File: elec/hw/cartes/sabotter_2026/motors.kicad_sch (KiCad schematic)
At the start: 3 parts

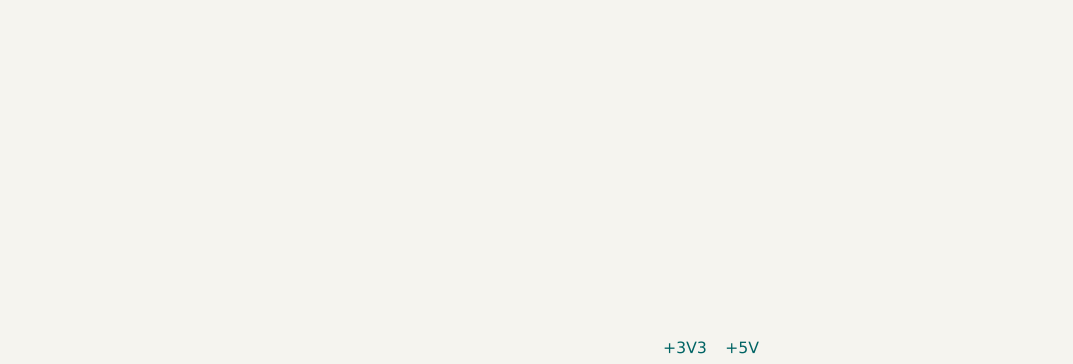
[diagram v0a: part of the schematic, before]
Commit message: switchs added to motor ribbon cable
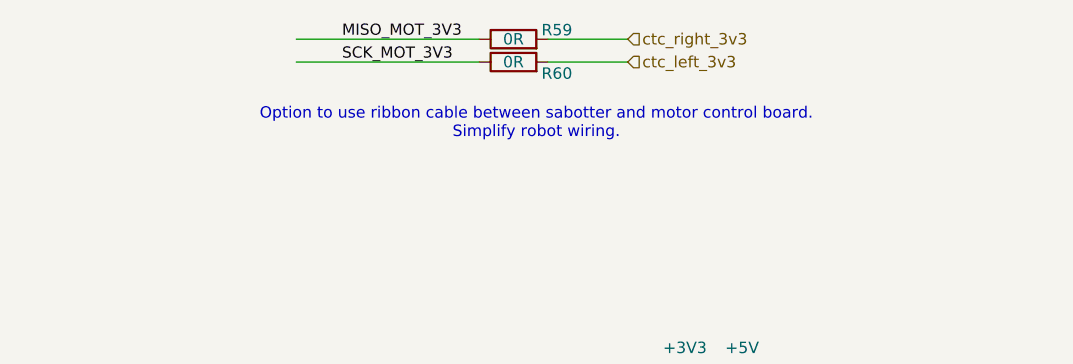
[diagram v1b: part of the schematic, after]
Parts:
- added R59, R60: 0R, cocotter_resistor:r0603_reflow, symbol cocotter_resistors:R_0R_0603
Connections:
- net miso_mot_3v3: now also R59.1
- net sck_mot_3v3: now also R60.1
- new net ctc_left_3v3: R60.2
- new net ctc_right_3v3: R59.2
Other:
- note added: "Option to use ribbon cable between sabotter and motor control board. Simplify robot wiring."

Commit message: sabotter wip
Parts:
- removed R59, R60: 0R, cocotter_resistor:r0603_reflow, symbol cocotter_resistors:R_0R_0603
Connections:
- net nCS_mot1_3v3 is gone; now on net scl_tof_3v3: J15.16 (nCS_3v3)
- net nCS_mot2_3v3 is gone; now on net scl_tof_3v3: J16.16 (nCS_3v3)
- net miso_mot_3v3 renamed irq0_3v3
- net mosi_mot_3v3 renamed irq1_3v3
- net nCS_mot0_3v3 renamed scl_tof_3v3
- net sck_mot_3v3 renamed sda_tof_3v3
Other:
- note removed: "Option to use ribbon cable between sabotter and motor control board. Simplify robot wiring."

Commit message: sabotter wip
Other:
- note added: "ou connecter les irq tof ?"
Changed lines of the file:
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@@
+		)
+	)
+	(text "ou connecter les irq tof ?\n"
+		(exclude_from_sim no)
+		(at 77.216 153.416 0)
+		(effects
+			(font
+				(size 1.27 1.27)
+			)
 		)
 	)

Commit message: tof irq added, needs routing
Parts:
- added R66, R67: 0R, cocotter_resistor:r0603_reflow, symbol cocotter_resistors:R_0R_0603
- added R68: 91k 1%, cocotter_resistor:r0603_reflow, symbol cocotter_resistors:R_91k_0603_1%
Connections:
- net +3V3: now also R68.1
- net irq0_3v3: now also R66.1
- net irq1_3v3: now also R67.1
- new net tof_irq_3v3: R66.2, R67.2, R68.2

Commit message: sabotter corrections wip
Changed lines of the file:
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@@
+		)
+	)
+	(label "irq1_3v3"
+		(at 149.86 116.84 0)
+		(effects
+			(font
+				(size 1.27 1.27)
+			)
+			(justify left bottom)
 		)
 	)
@@
 		)
 	)
+	(label "irq1_3v3"
+		(at 224.79 118.11 0)
+		(effects
+			(font
+				(size 1.27 1.27)
+			)
+			(justify left bottom)
+		)
+	)
 	(label "brake_mot_3v3"
 		(at 144.78 91.44 0)
@@
 		)
 	)
+	(label "irq0_3v3"
+		(at 224.79 115.57 0)
+		(effects
+			(font
+				(size 1.27 1.27)
+			)
+			(justify left bottom)
+		)
+	)
 	(label "GND"
 		(at 151.13 104.14 0)
@@
 			(font
 				(size 1.2446 1.2446)
+			)
+			(justify left bottom)
+		)
+	)
+	(label "irq0_3v3"
+		(at 149.86 114.3 0)
+		(effects
+			(font
+				(size 1.27 1.27)
 			)
 			(justify left bottom)
@@
 		)
 	)
-	(hierarchical_label "irq1_3v3"
-		(shape output)
-		(at 160.02 116.84 0)
-		(effects
-			(font
-				(size 1.27 1.27)
-			)
-			(justify left)
-		)
-	)
 	(hierarchical_label "scl_tof_3v3"
 		(shape input)
 		(at 53.34 121.92 0)
-		(effects
-			(font
-				(size 1.27 1.27)
-			)
-			(justify left)
-		)
-	)
-	(hierarchical_label "irq0_3v3"
-		(shape output)
-		(at 160.02 114.3 0)
-		(effects
-			(font
-				(size 1.27 1.27)
-			)
-			(justify left)
-		)
-	)
-	(hierarchical_label "irq0_3v3"
-		(shape output)
-		(at 237.49 115.57 0)
 		(effects
 			(font
@@
 		(effects
 			(font
-				(size 1.27 1.27)
-			)
-			(justify left)
-		)
-	)
-	(hierarchical_label "irq1_3v3"
-		(shape output)
-		(at 237.49 118.11 0)
-		(effects
-			(font

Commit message: sabotter corrected after review
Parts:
- R68: value 91k 1% -> 100k; symbol cocotter_resistors:R_91k_0603_1% -> cocotter_resistors:R_100k_0603_1%; JLCPCB Part # C23265 -> C25803; Specification 91k 0603 1% 100mW -> 100k 0603 1% 100mW; mouser (none) -> 603-RC0603FR-10100KL
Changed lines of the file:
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@@
 	)
 	(symbol
-		(lib_id "cocotter_resistors:R_91k_0603_1%")
+		(lib_id "cocotter_resistors:R_100k_0603_1%")
 		(at 68.58 49.53 0)
 		(unit 1)
@@
 			)
 		)
-		(property "Value" "91k 1%"
+		(property "Value" "100k"
 			(at 71.12 50.7999 0)
 			(effects
@@
 			)
 		)
-		(property "Specification" "91k 0603 1% 100mW"
+		(property "Specification" "100k 0603 1% 100mW"
 			(at 68.58 49.53 0)
 			(effects
@@
 			)
 		)
-		(property "mouser" ""
+		(property "mouser" "603-RC0603FR-10100KL"
 			(at 68.58 49.53 0)
 			(effects
@@
 			)
 		)
-		(property "JLCPCB Part #" "C23265"
+		(property "JLCPCB Part #" "C25803"
 			(at 68.58 49.53 0)
 			(effects
@@
 		(on_board yes)
 		(dnp no)
-		(fields_autoplaced yes)
 		(property "Reference" "R66"
-			(at 58.42 45.72 90)
+			(at 64.516 52.07 90)
 			(effects
 				(font
@@
 		)
 		(property "Value" "0R"
-			(at 58.42 48.26 90)
+			(at 58.42 52.07 90)
 			(effects
 				(font
@@
 		(on_board yes)
 		(dnp no)
-		(fields_autoplaced yes)
 		(property "Reference" "R67"
-			(at 58.42 49.53 90)
+			(at 64.516 55.88 90)
 			(effects
 				(font
@@
 		)
 		(property "Value" "0R"
-			(at 58.42 52.07 90)
-			(effects
-				(font
+			(at 58.42 55.88 90)
+			(effects
+				(font

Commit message: jlcpcb part added
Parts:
- J14, J15, J16: value ~ -> 1-188275-6; JLCPCB Part # (none) -> C720217
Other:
- note removed: "ou connecter les irq tof ?"
- moved on the sheet: J14, J15, J16
